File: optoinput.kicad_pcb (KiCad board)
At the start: 2 copper layers, 75.4 x 58.8 mm, 32 parts, among them P1 CONN_01X08, P2 CONN_01X08, P3 CONN_01X03, P6 CONN_01X02, U1 4N25, U2 4N25, U3 4N25, U4 4N25, U5 4N25, U6 4N25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

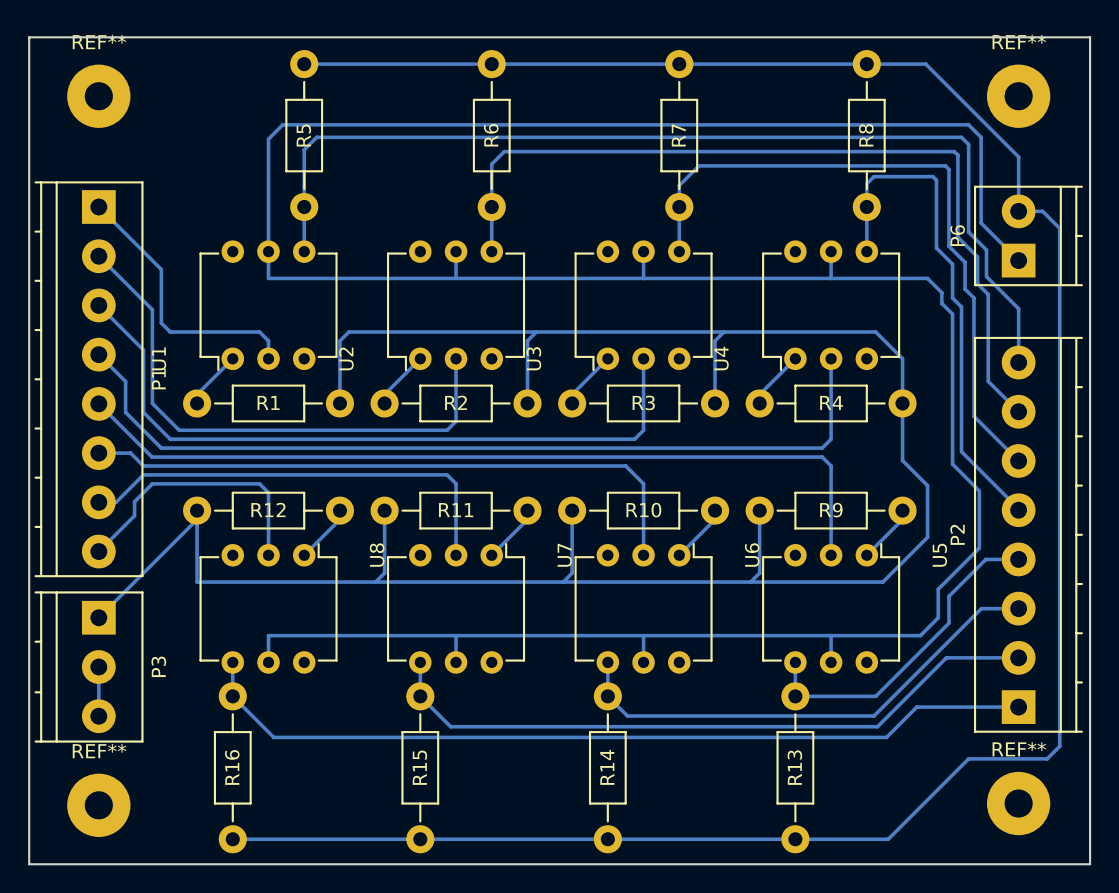
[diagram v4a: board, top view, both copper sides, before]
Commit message: Change position for screw holes (25mm for DIN rail mounting)
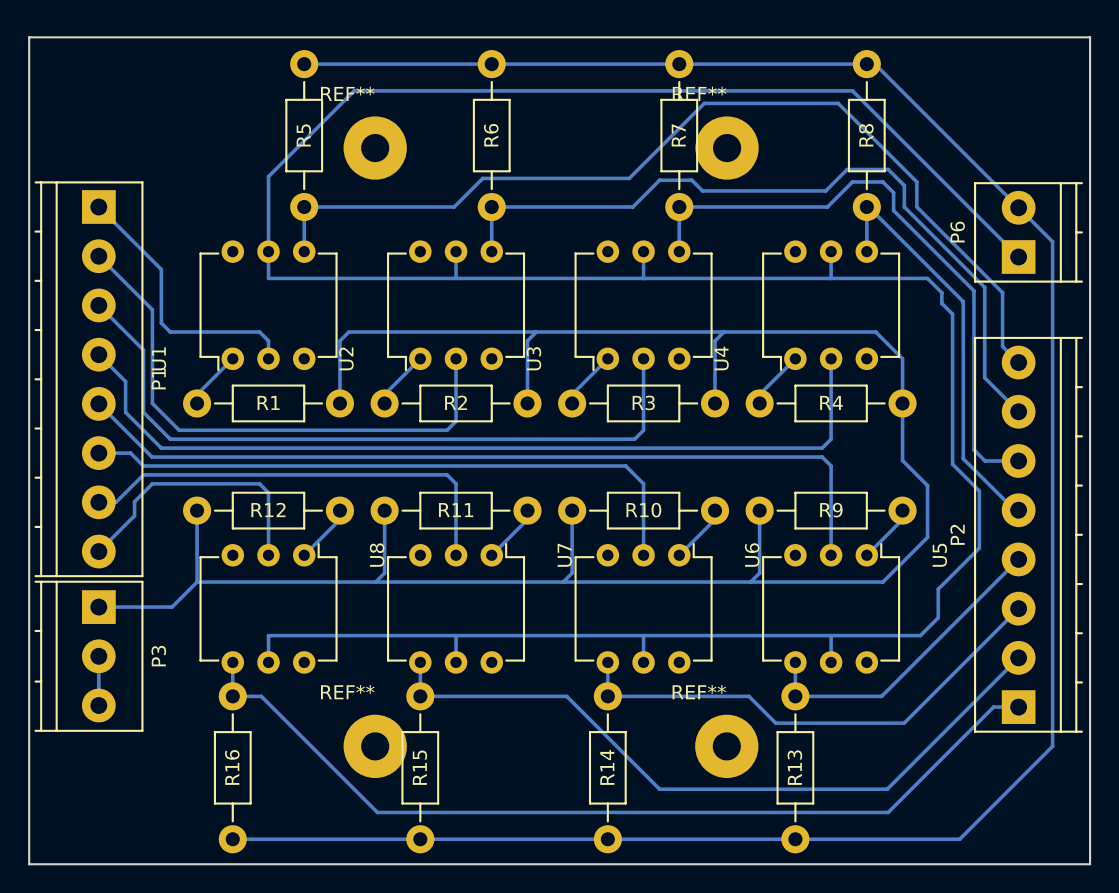
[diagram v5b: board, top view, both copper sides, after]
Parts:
- moved REF** 51.9 mm to (239.4, 97.7)
- moved REF** 51.5 mm to (239.4, 140.2)
- moved REF** 50.0 mm to (214.4, 97.7)
- moved REF** 49.5 mm to (214.4, 140.2)
- moved P3 0.76 mm to (196.7, 130.3)
- moved P6 0.25 mm to (262.1, 105.4)
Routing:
- net /Y4: track 36.0 -> 29.4 mm
- net /Y2: track 59.9 -> 54.2 mm
- net /Y8: track 60.4 -> 64.8 mm
- net /Y1: track 72.0 -> 67.9 mm
- net GND: track 159.2 -> 155.4 mm
- net /Y3: track 47.3 -> 43.6 mm
- net /Y7: track 47.9 -> 51.6 mm
- net VCC: track 206.5 -> 203.2 mm
- net +12V: track 154.5 -> 152.3 mm
- net /Y5: track 23.5 -> 22.3 mm
